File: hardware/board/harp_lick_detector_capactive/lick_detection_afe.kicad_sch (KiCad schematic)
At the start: 46 parts, among them J3 Conn_Triaxial, U13 ADS7049, U6 LTC6263, U7 LTC6268xS8-10, U8 REF2025

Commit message: draft v0.7 pcb schematic and layout
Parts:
- removed U6: LTC6263, Package_SO:MSOP-16_3x4mm_P0.5mm, symbol kicad_component_library:LTC6263
- added C29, C60, C64, C65, C66: 100nF, Capacitor_SMD:C_0402_1005Metric, symbol Device:C
- added R51, R53: 100K, Resistor_SMD:R_0402_1005Metric, symbol Device:R
- added U14, U6, U9: TS5A9411DCKR, Package_TO_SOT_SMD:SOT-363_SC-70-6, symbol kicad_component_library:TS5A9411DCKR
- added U15: LTC6081xMS8, Package_SO:MSOP-8_3x3mm_P0.65mm, symbol Amplifier_Operational:LTC6081xMS8
- added U16: AD8615, Package_TO_SOT_SMD:TSOT-23-5, symbol kicad_component_library:AD8615
- C30, C31: value 150pF -> 160pF; Link https://www.digikey.com/en/products/detail/murata-electronics/GCM1555C1H151FA16D/11618834 -> https://www.digikey.com/en/products/detail/murata-electronics/GCM1555C1H161FA16D/11618546; Manufacturer Number GCM1555C1H151FA16D -> GCM1555C1H161FA16D
- C33, C34: value 160pF -> 130pF; Link https://www.digikey.com/en/products/detail/murata-electronics/GCM1555C1H161FA16D/11618546 -> https://www.digikey.com/en/products/detail/murata-electronics/GCM1555C1H131FA16D/16033546; Manufacturer Number GCM1555C1H161FA16D -> GCM1555C1H131FA16D
- R18: value 105K -> 200K; Link https://www.digikey.com/en/products/detail/te-connectivity-passive-product/RP73PF1E105KBTD/8261055 -> https://www.digikey.com/en/products/detail/te-connectivity-passive-product/RP73PF1E200KBTD/8261082; Manufacturer Number RP73PF1E105KBTD -> RP73PF1E200KBTD
- R19, R49, R52: value 1K02 -> 1K00; Link https://www.digikey.com/en/products/detail/yageo/RT0402BRD0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 -> https://www.digikey.com/en/products/detail/yageo/RT0402BRB0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; Manufacturer Number RT0402BRD071K02L -> RT0402BRB071KL
- R20, R21, R22: value 102K -> 100K; Link https://www.digikey.com/en/products/detail/yageo/RT0402BRD07102KL/1068991 -> https://www.digikey.com/en/products/detail/yageo/RT0402BRD07100KL/1068989; Manufacturer Number RT0402BRD07102KL -> RT0402BRD07100KL
- R23: value 105K -> 249K; Link https://www.digikey.com/en/products/detail/te-connectivity-passive-product/RP73PF1E105KBTD/8261055 -> https://www.digikey.com/en/products/detail/te-connectivity-passive-product/RP73PF1E249KBTD/8261091; Manufacturer Number RP73PF1E105KBTD -> RP73PF1E249KBTD
- R24: value 1K05 -> 976; Link https://www.digikey.com/en/products/detail/yageo/RT0402BRD071K05L/1069088 -> https://www.digikey.com/en/products/detail/yageo/RT0402BRD07976RL/1069435; Manufacturer Number RT0402BRD071K05L -> RT0402BRD07976RL
- R26: value 102K -> 97K6; Link https://www.digikey.com/en/products/detail/yageo/RT0402BRD07102KL/1068991 -> https://www.digikey.com/en/products/detail/yageo/RT0402BRD0797K6L/1069436; Manufacturer Number RT0402BRD07102KL -> RT0402BRD0797K6L
- R27: value 9K53 -> 9K76; Link https://www.digikey.com/en/products/detail/yageo/RT0402BRD079K53L/1069441 -> https://www.digikey.com/en/products/detail/yageo/RT0402BRD079K76L/1069442; Manufacturer Number RT0402BRD079K53L -> RT0402BRD079K76L
- R46: value 124 -> 147; Link https://www.digikey.com/en/products/detail/yageo/RT0402BRE0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 -> https://www.digikey.com/en/products/detail/panasonic-electr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; Manufacturer Yageo -> Panasonic Electronic Components; Manufacturer Number RT0402BRE07124RL -> ERA-2AEB1470X
- R47: value 127 -> 140; Link https://www.digikey.com/en/products/detail/yageo/RT0402BRD07127RL/1069018 -> https://www.digikey.com/en/products/detail/yageo/RT0402BRD07140RL/1069036; Manufacturer Number RT0402BRD07127RL -> RT0402BRD07140RL
- R48: value 9K76 -> 8K66; Link https://www.digikey.com/en/products/detail/yageo/RT0402BRD079K76L/1069442 -> https://www.digikey.com/en/products/detail/yageo/RT0402BRD078K66L/1069421; Manufacturer Number RT0402BRD079K76L -> RT0402BRD078K66L
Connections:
- net +2V5: now also C65.2, U15.8 (V+), U16.5 (V+)
- net +3V3: now also C29.2, C60.2, C64.2, U14.2 (Vcc), U6.2 (Vcc), U9.2 (Vcc)
- net -2V5: now also C66.1, U15.4 (V-), U16.2 (V-)
- net GND: now also C29.1, C60.1, C64.1, C65.1, C66.2, R53.2, U14.3 (GND), U6.3 (GND), U9.3 (GND)
- net VREF_1V25: now also R21.1; no longer R21.2
- net at R49.1: now also U9.4; no longer R21.1
- net at C33.2, R26.2, R48.2: now also U14.6, U15.1; no longer R49.2
- net at R22.2: now also R43.2, TP1.1, U16.1; no longer R52.1
- net at R47.2, R48.1: now also U15.3 (+)
- net at R15.2, R18.1, U7.2 (-)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: now also R23.1
- net at C34.2, R26.1: now also U15.2 (-)
- net at C30.2, R20.2, R27.2: now also U14.4, U15.7; no longer R23.1
- net at C31.2, R20.1: now also U15.6 (-)
- net at R27.1, R46.2: now also U15.5 (+)
- new net: R21.2, U16.3 (+), U9.5
- new net: R51.1, U9.6
- new net: R22.1, U16.4 (-), U6.5
- new net: R52.1, U6.4
- new net: R53.1, U6.6
- new net: R49.2, R51.2, U14.5
- new net FILTER_SEL: U14.1
- new net GAIN_SEL: U6.1, U9.1
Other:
- note added: "100KHz 2nd Order Bandpass Filter"
- note added: "100x-or-1x Gain Amplifier with +1.25V DC offset"
- note added: "125KHz 2nd Order Bandpass Filter"
- note added: "2.5V Full Scale Range"
- note added: "Note: LTC6268 input is ESD protected."
- note added: "Note: this setup must be grounded to the animal at a single point using (1) H1, (2) the outer shield of J3's cable, or (3) the PSU power supply GND. (i.e: current must flow out of the lick detector water delivery spout, through the animal's tongue, to ground. The sensing element must be connected to a conductive water delivery spout.)"
- note added: "U15 Bypass Caps"
- note added: "U16 Bypass Caps"
- note added: "U7 Bypass Caps"
- note added: "U8 Bypass Caps"
- note removed: "100x Inverting Amplification +1.25V DC offset"
- note removed: "4th Order Bandpass Filter"
- note removed: "Bypass Caps"
- note removed: "Note: LTC6268 and LTC6263 inputs are ESD protected."
- note removed: "Note: this setup must be grounded to the animal at a single point using either H1 or the outer shield of J3's cable. (i.e: current must flow out of the lick detector water delivery spout, through the animal's tongue, to ground. The sensing element is connected to a conductive water delivery spout.)"
- note removed: "REF2033 Bypass Caps"
- note removed: "TODO: consider common mode choke for connector inputs. 3-line: EXC-16CT350U"
- moved on the sheet: C20, C21, C22, C23, C24, C25, C26, C28, C34, C38, C59, C8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

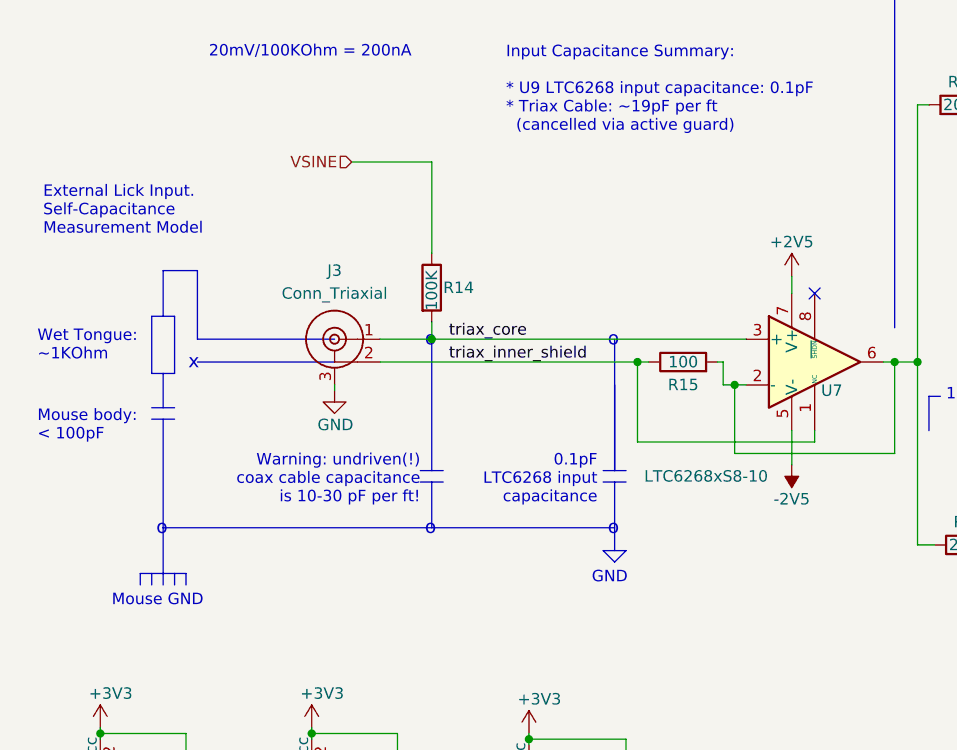
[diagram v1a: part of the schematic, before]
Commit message: implement soe feedback in layout
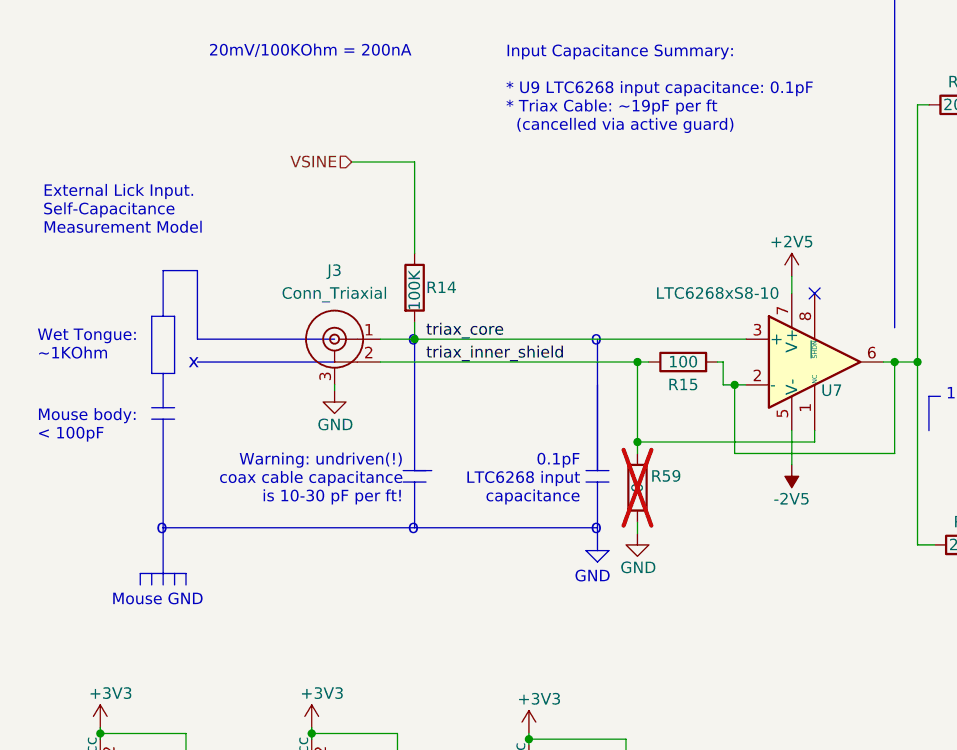
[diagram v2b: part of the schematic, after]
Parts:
- added R59: 0, Resistor_SMD:R_0402_1005Metric_Pad0.72x0.64mm_HandSolder, symbol Device:R
- U14, U6, U9: Link (none) -> https://www.digikey.com/en/products/detail/texas-instrument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; Manufacturer (none) -> Texas Instruments; Manufacturer Number (none) -> TS5A9411DCKR
- U16: Link (none) -> https://www.digikey.com/en/products/detail/analog-devices-i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; Manufacturer (none) -> Analog Devices Inc.; Manufacturer Number (none) -> AD8615AUJZ-R2
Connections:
- net GND: now also R59.1
- net triax_inner_shield: now also R59.2
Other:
- moved on the sheet: R14

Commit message: draft v0.8 pcb layout
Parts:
- removed C66: 100nF, Capacitor_SMD:C_0402_1005Metric, symbol Device:C
- removed U14, U6: TS5A9411DCKR, Package_TO_SOT_SMD:SOT-363_SC-70-6, symbol kicad_component_library:TS5A9411DCKR
- removed U15: LTC6081xMS8, Package_SO:MSOP-8_3x3mm_P0.65mm, symbol Amplifier_Operational:LTC6081xMS8
- removed U16: AD8615, Package_TO_SOT_SMD:TSOT-23-5, symbol kicad_component_library:AD8615
- added C68, C72: 160pF, Capacitor_SMD:C_0402_1005Metric, symbol Device:C
- added C69, C70: 100nF, Capacitor_SMD:C_0402_1005Metric, symbol Device:C
- added C73, C74: 130pF, Capacitor_SMD:C_0402_1005Metric, symbol Device:C
- added R62, R63, R65: 1K00, Resistor_SMD:R_0402_1005Metric, symbol Device:R
- added R64: 200K, Resistor_SMD:R_0402_1005Metric, symbol Device:R
- added R66: 100K, Resistor_SMD:R_0402_1005Metric, symbol Device:R
- added R67: 9K76, Resistor_SMD:R_0402_1005Metric, symbol Device:R
- added R68: 147, Resistor_SMD:R_0402_1005Metric, symbol Device:R
- added R69: 249K, Resistor_SMD:R_0402_1005Metric, symbol Device:R
- added R70: 976, Resistor_SMD:R_0402_1005Metric, symbol Device:R
- added R71: 97K6, Resistor_SMD:R_0402_1005Metric, symbol Device:R
- added R72: 8K66, Resistor_SMD:R_0402_1005Metric, symbol Device:R
- added R73: 140, Resistor_SMD:R_0402_1005Metric, symbol Device:R
- added U10: AD8652, Package_SO:MSOP-8_3x3mm_P0.65mm, symbol kicad_component_library:AD8652
- added U14: MAX4564EKA, Package_TO_SOT_SMD:SOT-23-8, symbol kicad_component_library:MAX4564EKA+T
- added U6: ADA4891-4, Package_SO:TSSOP-14_4.4x5mm_P0.65mm, symbol kicad_component_library:ADA4891-4
- R51, R53: value 100K -> 1K00; Link https://www.digikey.com/en/products/detail/yageo/RT0402BRD0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 -> https://www.digikey.com/en/products/detail/yageo/RT0402BRB0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; Manufacturer Number RT0402BRD07100KL -> RT0402BRB071KL
- U9: Link https://www.digikey.com/en/products/detail/texas-instrument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 -> (none); Manufacturer Texas Instruments -> (none); Manufacturer Number TS5A9411DCKR -> (none)
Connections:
- net +2V5: now also C29.1, C64.2, U10.8 (V+), U14.2 (V+), U6.4 (V+); no longer C65.2
- net -2V5: now also C69.1, C70.1, U10.4 (V-), U14.6 (V-), U6.11 (V-)
- net GND: now also C29.2, R52.1, C69.2, C70.2, R65.1, R68.1, R70.1, R73.1, U14.5 (GND), U14.7 (~{EN}); no longer C29.1, R52.2
- net VREF_1V25: now also C65.2, R63.1
- net at R21.2: now also R51.1, U10.3 (+); no longer U9.5
- net at U9.4: now also R22.2, U10.1; no longer R49.1
- net at U9.6: now also R62.2, U10.7; no longer R51.1
- net at R47.2, R48.1: now also U6.3 (+)
- net at C33.2, R26.2, R48.2: now also R69.2, U6.1
- net at R22.1: now also R53.1, U10.2 (-)
- net at R43.2, TP1.1: now also U9.5; no longer R22.2
- net at R15.2, R18.1, U7.2 (-)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: now also R23.2; no longer R23.1
- net at C33.1, C34.1, R24.2: now also R23.1; no longer R23.2
- net at C34.2, R26.1: now also U6.2 (-)
- net at R27.1, R46.2: now also U6.12 (+)
- net at C30.2, R20.2, R27.2: now also R64.2, U6.14
- net at R51.2: now also R49.1, U14.8; no longer R49.2
- net at C31.2, R20.1: now also U6.13 (-)
- net +3V3 renamed +3.3V
- net +3.3V: no longer C29.2, C64.2
- new net: R72.1, R73.2, U6.5 (+)
- new net: C74.2, R71.1, U6.6 (-)
- new net: C73.2, R71.2, R72.2, U14.4, U6.7
- new net: R67.1, R68.2, U6.10 (+)
- new net: C68.1, C72.1, R64.1, R65.2
- new net: C68.2, R66.2, R67.2, U14.1, U6.8
- new net: C72.2, R66.1, U6.9 (-)
- new net: R52.2, R62.1, U10.6 (-)
- new net: R49.2, R63.2, U10.5 (+)
- new net: C73.1, C74.1, R69.1, R70.2
- new net FREQ_SEL_2V5: U14.3
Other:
- note added: "100KHz 4th Order Bandpass Filter"
- note added: "100x-or-1x Gain Amplification with +1.25V DC offset"
- note added: "125KHz 4th Order Bandpass Filter"
- note added: "Input Capacitance Summary: * LTC6268 input capacitance: 0.1pF * Triax Cable: ~19pF per ft (cancelled via active guard)"
- note added: "Place C38 near R21. Place C65 near R63."
- note added: "TODO: update resistor and capacitor values in Bandpass filters. TODO: 0603 100nF capacitors for 4x op-amp"
- note added: "Warning: undriven(!)coax cable capacitance is 10-30 pF per ft!"
- note removed: "100KHz 2nd Order Bandpass Filter"
- note removed: "100x-or-1x Gain Amplifier with +1.25V DC offset"
- note removed: "125KHz 2nd Order Bandpass Filter"
- note removed: "Input Capacitance Summary: * U9 LTC6268 input capacitance: 0.1pF * Triax Cable: ~19pF per ft (cancelled via active guard)"
- note removed: "Place C38 near R21."
- note removed: "U16 Bypass Caps"
- note removed: "Warning: undriven(!) coax cable capacitance is 10-30 pF per ft!"
- moved on the sheet: C20, C21, C22, C23, C24, C25, C26, C28, C29, C30, C31, C33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

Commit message: update board with filter resistor values
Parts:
- C24, C25: footprint Capacitor_SMD:C_0402_1005Metric -> Capacitor_SMD:C_0603_1608Metric; Link https://www.digikey.com/en/products/detail/walsin-technolog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 -> https://www.digikey.com/en/products/detail/samsung-electro-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; Manufacturer Walson Technology Corporation -> Samsung Electro-Mechanics; Manufacturer Number 0402B104K160CT -> CL10B104KB8NNNC; Rated Voltage 16V -> 50V
- C33, C34: value 130pF -> 120pF; Link https://www.digikey.com/en/products/detail/murata-electronics/GCM1555C1H131FA16D/16033546 -> https://www.digikey.com/en/products/detail/murata-electronics/GCM1555C1H121FA16D/7363202; Manufacturer Number GCM1555C1H131FA16D -> GCM1555C1H121FA16D
- R18: value 200K -> 127K; Link https://www.digikey.com/en/products/detail/te-connectivity-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 -> https://www.digikey.com/en/products/detail/yageo/RT0402BRD0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; Manufacturer TE Connectivity Passive Product -> Yageo; Manufacturer Number RP73PF1E200KBTD -> RT0402BRD07127KL
- R19: value 1K00 -> 976; Link https://www.digikey.com/en/products/detail/yageo/RT0402BRB0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 -> https://www.digikey.com/en/products/detail/yageo/RT0402BRD0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; Manufacturer Number RT0402BRB071KL -> RT0402BRD07976RL
- R20: value 100K -> 97K6; Link https://www.digikey.com/en/products/detail/yageo/RT0402BRD07100KL/1068989 -> https://www.digikey.com/en/products/detail/yageo/RT0402BRD0797K6L/1069436; Manufacturer Number RT0402BRD07100KL -> RT0402BRD0797K6L
- R23: value 249K -> 127K; Link https://www.digikey.com/en/products/detail/te-connectivity-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 -> https://www.digikey.com/en/products/detail/yageo/RT0402BRD0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; Manufacturer TE Connectivity Passive Product -> Yageo; Manufacturer Number RP73PF1E249KBTD -> RT0402BRD07127KL
- R24: value 976 -> 1K05; Link https://www.digikey.com/en/products/detail/yageo/RT0402BRD07976RL/1069435 -> https://www.digikey.com/en/products/detail/yageo/RT0402BRD071K05L/1069088; Manufacturer Number RT0402BRD07976RL -> RT0402BRD071K05L
- R26: value 97K6 -> 102K; Link https://www.digikey.com/en/products/detail/yageo/RT0402BRD0797K6L/1069436 -> https://www.digikey.com/en/products/detail/yageo/RT0402BRD07102KL/1068991; Manufacturer Number RT0402BRD0797K6L -> RT0402BRD07102KL
- R27: value 9K76 -> 10K0; Link https://www.digikey.com/en/products/detail/yageo/RT0402BRD0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 -> https://www.digikey.com/en/products/detail/stackpole-electr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; Manufacturer Yageo -> Stackpole Electronics Inc; Manufacturer Number RT0402BRD079K76L -> RNCF0402BTE10K0
- R46: value 147 -> 133; Link https://www.digikey.com/en/products/detail/panasonic-electr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 -> https://www.digikey.com/en/products/detail/yageo/RT0402BRD0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; Manufacturer Panasonic Electronic Components -> Yageo; Manufacturer Number ERA-2AEB1470X -> RT0402BRD07133RL
- R47: value 140 -> 113; Link https://www.digikey.com/en/products/detail/yageo/RT0402BRD07140RL/1069036 -> https://www.digikey.com/en/products/detail/yageo/RT0402BRD07113RL/1069004; Manufacturer Number RT0402BRD07140RL -> RT0402BRD07113RL
- R48, R72: value 8K66 -> 8K87; Link https://www.digikey.com/en/products/detail/yageo/RT0402BRD078K66L/1069421 -> https://www.digikey.com/en/products/detail/yageo/RT0402BRD078K87L/1069422; Manufacturer Number RT0402BRD078K66L -> RT0402BRD078K87L
- R64: value 200K -> 133K; Link https://www.digikey.com/en/products/detail/te-connectivity-passive-product/RP73PF1E200KBTD/8261082 -> https://www.digikey.com/en/products/detail/te-connectivity-passive-product/RP73PF1E133KBTD/8261065; Manufacturer Number RP73PF1E200KBTD -> RP73PF1E133KBTD
- R65: value 1K00 -> 1K02; Link https://www.digikey.com/en/products/detail/yageo/RT0402BRB0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 -> https://www.digikey.com/en/products/detail/yageo/RT0402BRD0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; Manufacturer Number RT0402BRB071KL -> RT0402BRD071K02L
- R67: value 9K76 -> 10K2; Link https://www.digikey.com/en/products/detail/yageo/RT0402BRD079K76L/1069442 -> https://www.digikey.com/en/products/detail/yageo/RT0402BRD0710K2L/1068995; Manufacturer Number RT0402BRD079K76L -> RT0402BRD0710K2L
- R68: value 147 -> 137; Link https://www.digikey.com/en/products/detail/panasonic-electronic-components/ERA-2AEB1470X/3063682 -> https://www.digikey.com/en/products/detail/panasonic-electronic-components/ERA-2AEB1370X/2025974; Manufacturer Number ERA-2AEB1470X -> ERA-2AEB1370X
- R69: value 249K -> 121K; Link https://www.digikey.com/en/products/detail/te-connectivity-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 -> https://www.digikey.com/en/products/detail/yageo/RT0402BRD0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; Manufacturer TE Connectivity Passive Product -> Yageo; Manufacturer Number RP73PF1E249KBTD -> RT0402BRD07121KL
- R70: value 976 -> 1K00; Link https://www.digikey.com/en/products/detail/yageo/RT0402BRD0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 -> https://www.digikey.com/en/products/detail/yageo/RT0402BRB0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; Manufacturer Number RT0402BRD07976RL -> RT0402BRB071KL
- R71: value 97K6 -> 100K; Link https://www.digikey.com/en/products/detail/yageo/RT0402BRD0797K6L/1069436 -> https://www.digikey.com/en/products/detail/yageo/RT0402BRD07100KL/1068989; Manufacturer Number RT0402BRD0797K6L -> RT0402BRD07100KL
- R73: value 140 -> 115; Link https://www.digikey.com/en/products/detail/yageo/RT0402BRD0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 -> https://www.digikey.com/en/products/detail/panasonic-electr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; Manufacturer Yageo -> Panasonic Electronic Components; Manufacturer Number RT0402BRD07140RL -> ERA-2AEB1150X
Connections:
- net GND: now also R47.2, R70.2; no longer R47.1, R70.1
- net at R48.1, U6.3 (+): now also R47.1; no longer R47.2
- net at C73.1, C74.1, R69.1: now also R70.1; no longer R70.2
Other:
- note removed: "TODO: update resistor and capacitor values in Bandpass filters. TODO: 0603 100nF capacitors for 4x op-amp"
